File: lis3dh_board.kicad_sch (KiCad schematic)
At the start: 19 parts, among them J1 T4_IF, J2 BQ25798_BOARD, J3 WL-125, Q1 BSS138, U1 TLV75530PDBV, U2 LIS3DH

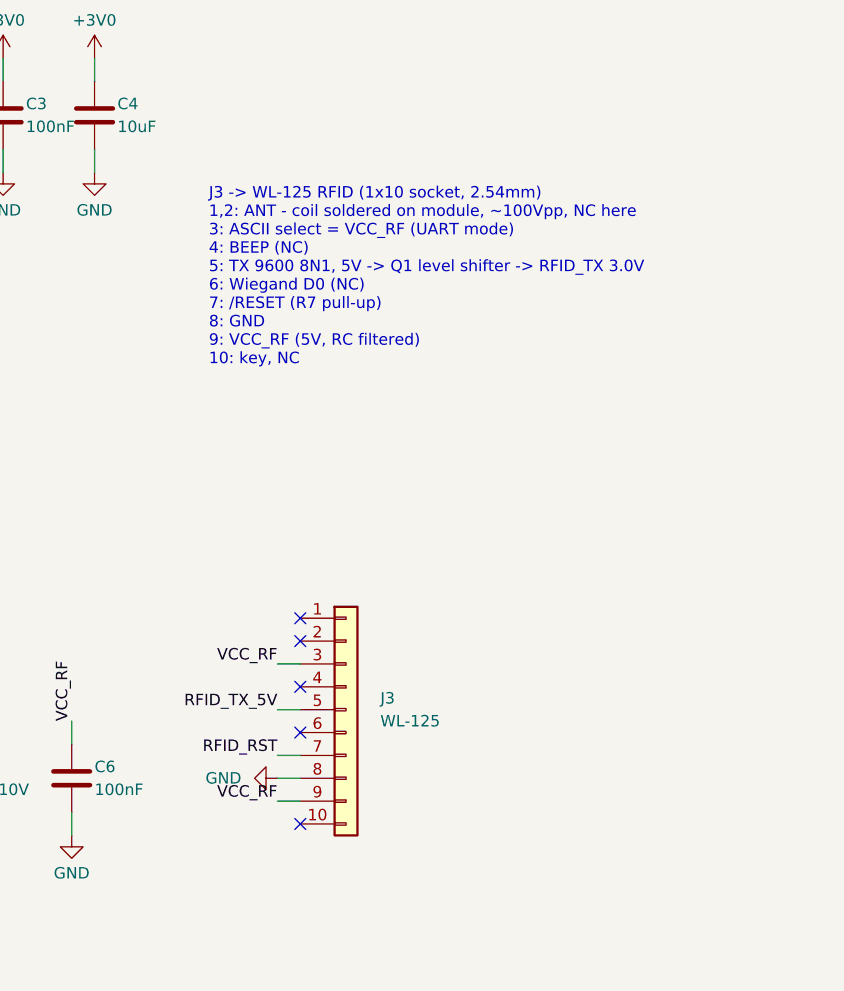
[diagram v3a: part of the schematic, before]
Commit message: Put the WL-125 polarization key next to module pin 1
J3 pin 1 is now the key position and module pins 1-9 map to J3 pins
2-10, matching how the module's 10-pin header is fitted.

Co-Authored-By: Claude Opus 5.5 <noreply@anthropic.com>
Claude-Session: https://claude.ai/code/session_012K15v8QNdkAoa4NiCNiWuG
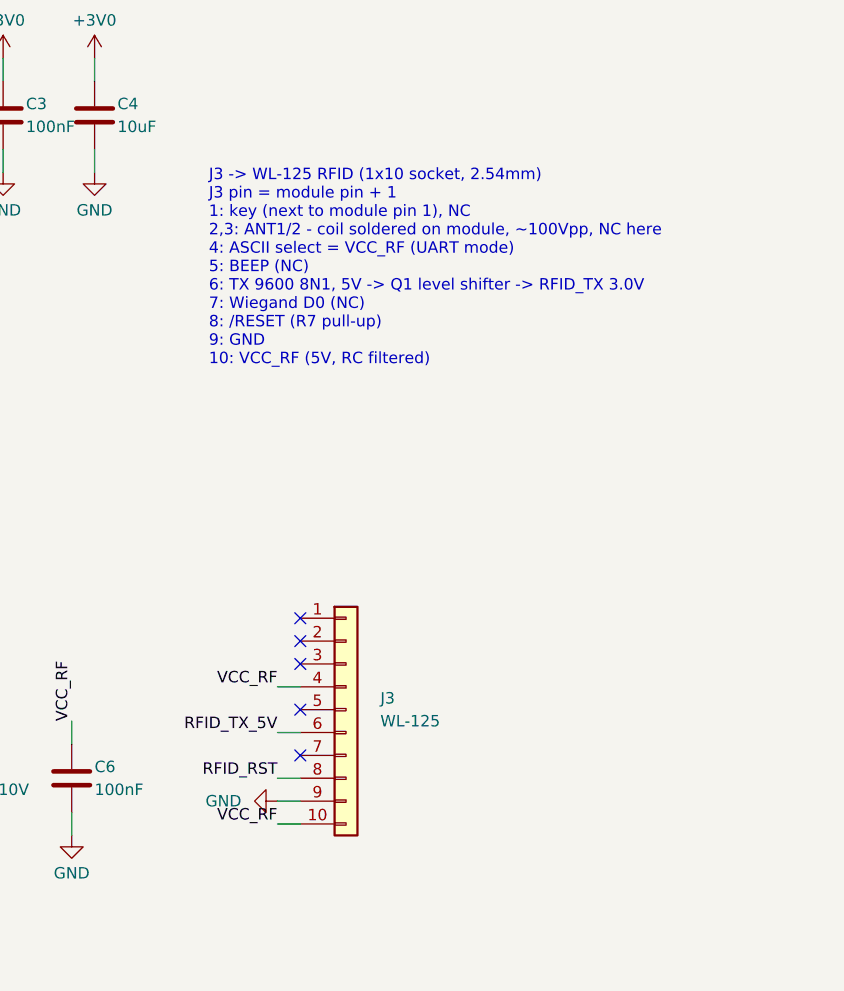
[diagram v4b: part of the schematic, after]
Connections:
- net GND: now also J3.9 (Pin_9); no longer J3.8 (Pin_8)
- net RFID_RST: now also J3.8 (Pin_8); no longer J3.7 (Pin_7)
- net RFID_TX_5V: now also J3.6 (Pin_6); no longer J3.5 (Pin_5)
- net VCC_RF: now also J3.10 (Pin_10), J3.4 (Pin_4); no longer J3.3 (Pin_3), J3.9 (Pin_9)
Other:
- note added: "J3 -> WL-125 RFID (1x10 socket, 2.54mm) J3 pin = module pin + 1 1: key (next to module pin 1), NC 2,3: ANT1/2 - coil soldered on module, ~100Vpp, NC here 4: ASCII select = VCC_RF (UART mode) 5: BEEP (NC) 6: TX 9600 8N1, 5V -> Q1 level shifter -> RFID_TX 3.0V 7: Wiegand D0 (NC) 8: /RESET (R7 pull-up) 9: GND 10: VCC_RF (5V, RC filtered)"
- note removed: "J3 -> WL-125 RFID (1x10 socket, 2.54mm) 1,2: ANT - coil soldered on module, ~100Vpp, NC here 3: ASCII select = VCC_RF (UART mode) 4: BEEP (NC) 5: TX 9600 8N1, 5V -> Q1 level shifter -> RFID_TX 3.0V 6: Wiegand D0 (NC) 7: /RESET (R7 pull-up) 8: GND 9: VCC_RF (5V, RC filtered) 10: key, NC"
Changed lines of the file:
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@@
   (no_connect (at 223.52 134.62))
   (no_connect (at 223.52 137.16))
-  (wire (pts (xy 223.52 139.7) (xy 220.98 139.7))
+  (no_connect (at 223.52 139.7))
+  (wire (pts (xy 223.52 142.24) (xy 220.98 142.24))
     (stroke (width 0) (type default))
   )
-  (label "VCC_RF" (at 220.98 139.7 180) (fields_autoplaced)
+  (label "VCC_RF" (at 220.98 142.24 180) (fields_autoplaced)
     (effects (font (size 1.27 1.27)) (justify right bottom))
   )
-  (no_connect (at 223.52 142.24))
-  (wire (pts (xy 223.52 144.78) (xy 220.98 144.78))
+  (no_connect (at 223.52 144.78))
+  (wire (pts (xy 223.52 147.32) (xy 220.98 147.32))
     (stroke (width 0) (type default))
   )
-  (label "RFID_TX_5V" (at 220.98 144.78 180) (fields_autoplaced)
+  (label "RFID_TX_5V" (at 220.98 147.32 180) (fields_autoplaced)
     (effects (font (size 1.27 1.27)) (justify right bottom))
   )
-  (no_connect (at 223.52 147.32))
-  (wire (pts (xy 223.52 149.86) (xy 220.98 149.86))
-    (stroke (width 0) (type default))
-  )
-  (label "RFID_RST" (at 220.98 149.86 180) (fields_autoplaced)
-    (effects (font (size 1.27 1.27)) (justify right bottom))
-  )
+  (no_connect (at 223.52 149.86))
   (wire (pts (xy 223.52 152.4) (xy 220.98 152.4))
     (stroke (width 0) (type default))
   )
-  (symbol (lib_id "power:GND") (at 220.98 152.4 270) (unit 1)
+  (label "RFID_RST" (at 220.98 152.4 180) (fields_autoplaced)
+    (effects (font (size 1.27 1.27)) (justify right bottom))
+  )
+  (wire (pts (xy 223.52 154.94) (xy 220.98 154.94))
+    (stroke (width 0) (type default))
+  )
+  (symbol (lib_id "power:GND") (at 220.98 154.94 270) (unit 1)
     (in_bom no) (on_board no) (dnp no)
-    (property "Reference" "#PWR019" (at 220.98 158.4 0)
+    (property "Reference" "#PWR019" (at 220.98 160.94 0)
       (effects (font (size 1.27 1.27)) hide)
     )
-    (property "Value" "GND" (at 216.98 152.4 270)
+    (property "Value" "GND" (at 216.98 154.94 270)
       (effects (font (size 1.27 1.27)) (justify left))
     )
-    (property "Footprint" "" (at 220.98 152.4 0)
+    (property "Footprint" "" (at 220.98 154.94 0)
       (effects (font (size 1.27 1.27)) hide)
     )
-    (property "Datasheet" "~" (at 220.98 152.4 0)
+    (property "Datasheet" "~" (at 220.98 154.94 0)
       (effects (font (size 1.27 1.27)) hide)
     )
@@
     )
   )
-  (wire (pts (xy 223.52 154.94) (xy 220.98 154.94))
+  (wire (pts (xy 223.52 157.48) (xy 220.98 157.48))
     (stroke (width 0) (type default))
   )
-  (label "VCC_RF" (at 220.98 154.94 180) (fields_autoplaced)
+  (label "VCC_RF" (at 220.98 157.48 180) (fields_autoplaced)
     (effects (font (size 1.27 1.27)) (justify right bottom))
   )
-  (no_connect (at 223.52 157.48))
-  (text "J3 -> WL-125 RFID (1x10 socket, 2.54mm)\n1,2: ANT - coil soldered on module, ~100Vpp, NC here\n3: ASCII select = VCC_RF (UART mode)\n4: BEEP (NC)\n5: TX 9600 8N1, 5V -> Q1 level shifter -> RFID_TX 3.0V\n6: Wiegand D0 (NC)\n7: /RESET (R7 pull-up)\n8: GND\n9: VCC_RF (5V, RC filtered)\n10: key, NC" (at 213.36 106.68 0)
+  (text "J3 -> WL-125 RFID (1x10 socket, 2.54mm)\nJ3 pin = module pin + 1\n1: key (next to module pin 1), NC\n2,3: ANT1/2 - coil soldered on module, ~100Vpp, NC here\n4: ASCII select = VCC_RF (UART mode)\n5: BEEP (NC)\n6: TX 9600 8N1, 5V -> Q1 level shifter -> RFID_TX 3.0V\n7: Wiegand D0 (NC)\n8: /RESET (R7 pull-up)\n9: GND\n10: VCC_RF (5V, RC filtered)" (at 213.36 106.68 0)
     (effects (font (size 1.27 1.27)) (justify left bottom))
   )

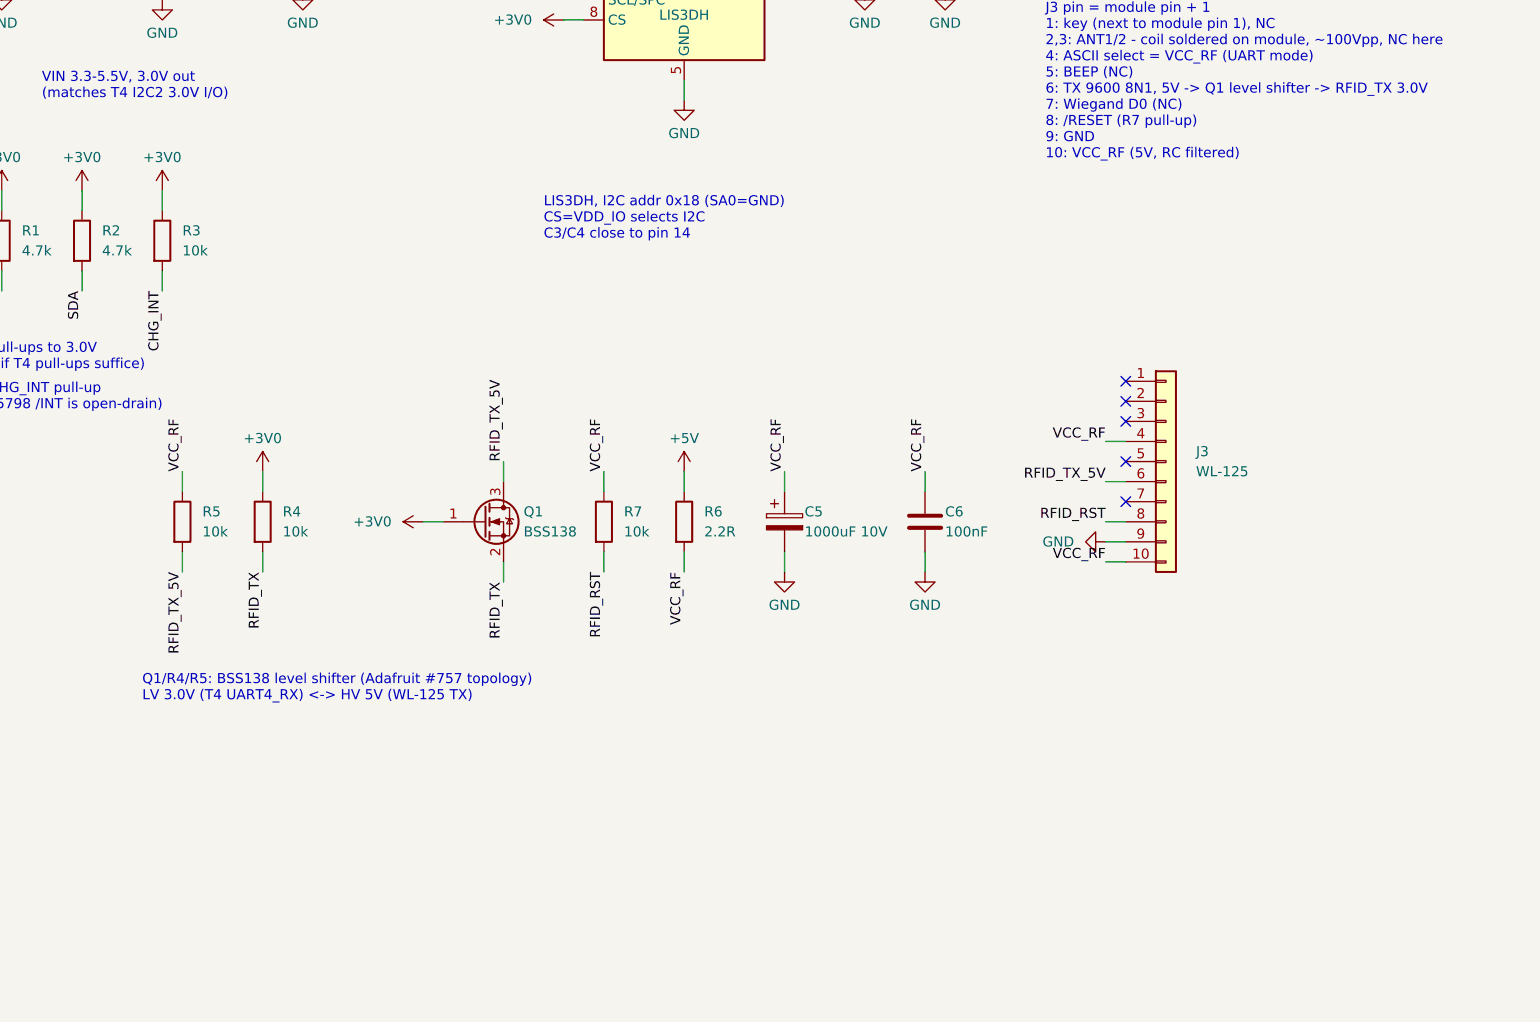
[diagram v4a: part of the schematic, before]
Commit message: Use a 3-stage RC filter for the WL-125 supply
+5V -> 4.7R -> 1000uF -> 1R -> 1000uF -> 1R -> 1000uF + 100nF ->
VCC_RF, following the WL-125 datasheet appendix. The first resistor is
4.7R to keep the inrush into 3 x 1000uF around 1A, and the 100nF covers
frequencies where the electrolytics stop working. Sheet moved to A3 to
fit the filter.

Co-Authored-By: Claude Opus 5.5 <noreply@anthropic.com>
Claude-Session: https://claude.ai/code/session_012K15v8QNdkAoa4NiCNiWuG
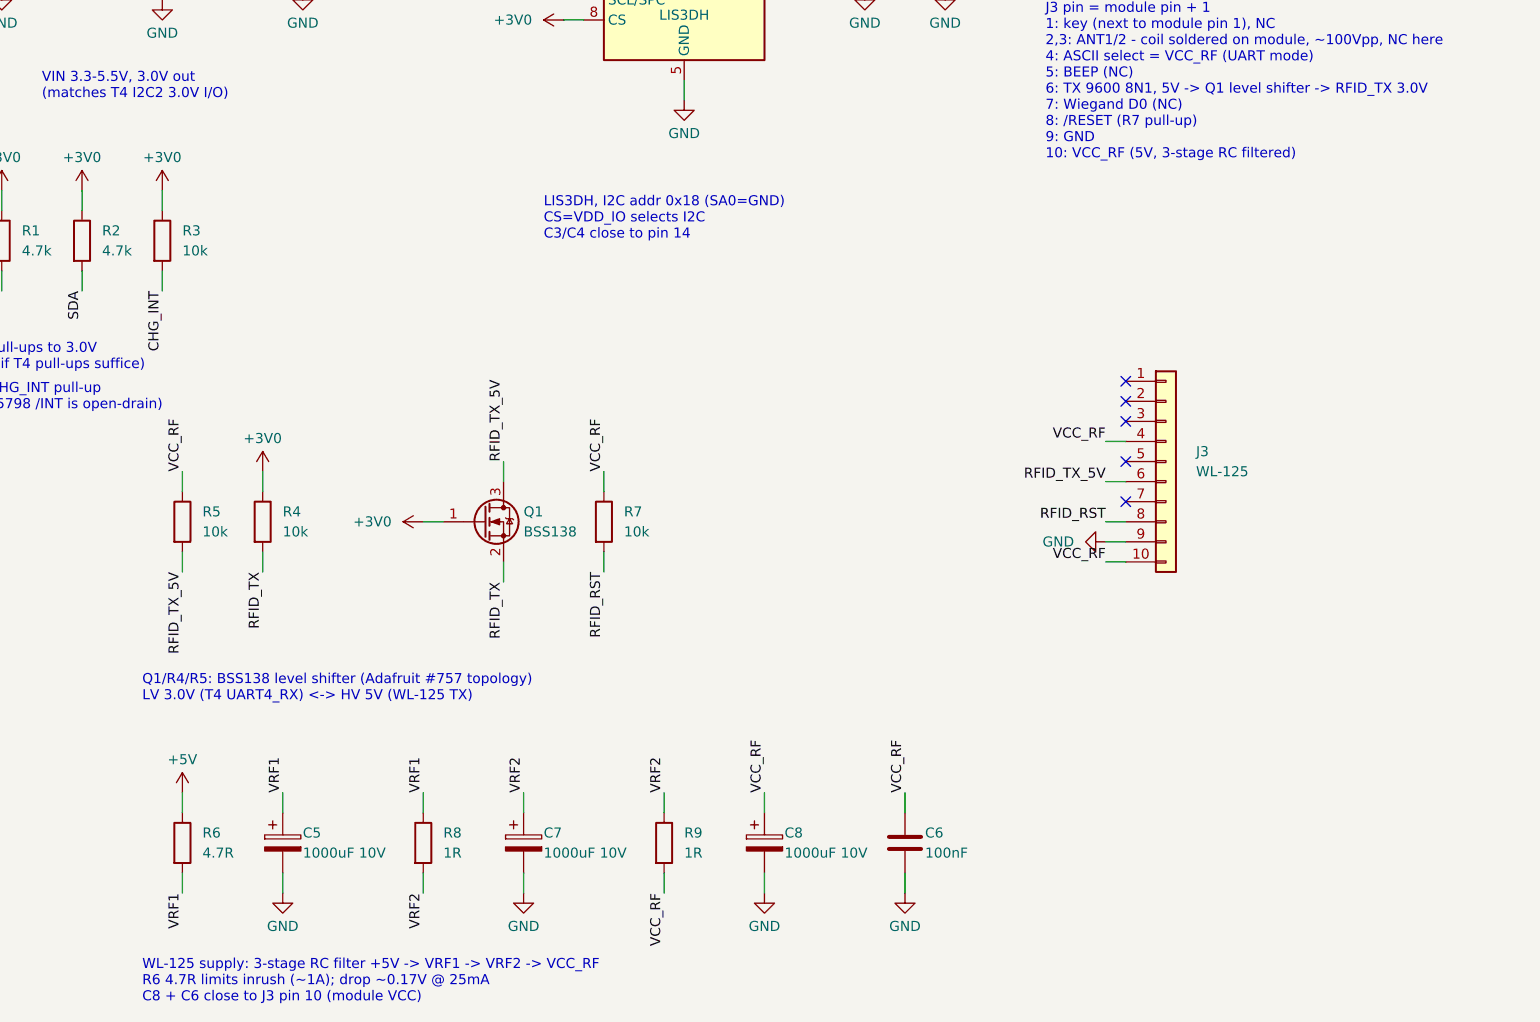
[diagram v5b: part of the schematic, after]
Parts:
- added C6: 100nF, Capacitor_SMD:C_0603_1608Metric, symbol Device:C
- added C7: 1000uF 10V, Capacitor_THT:CP_Radial_D10.0mm_P5.00mm, symbol Device:C_Polarized
- added R9: 1R, Resistor_SMD:R_0805_2012Metric, symbol Device:R
- added U2: LIS3DH, Package_LGA:LGA-16_3x3mm_P0.5mm_LayoutBorder3x5y, symbol Sensor_Motion:LIS3DH
- C8: renamed from U2; value LIS3DH -> 1000uF 10V; footprint Package_LGA:LGA-16_3x3mm_P0.5mm_LayoutBorder3x5y -> Capacitor_THT:CP_Radial_D10.0mm_P5.00mm; symbol Sensor_Motion:LIS3DH -> Device:C_Polarized
- R6: value 2.2R -> 4.7R
- R8: renamed from C6; value 100nF -> 1R; footprint Capacitor_SMD:C_0603_1608Metric -> Resistor_SMD:R_0805_2012Metric; symbol Device:C -> Device:R
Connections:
- net +3V0: now also U2.1 (VDD_IO), U2.14 (VDD), U2.8 (CS); no longer C8.1 (VDD_IO), C8.14 (VDD), C8.8 (CS)
- net GND: now also C8.2, C6.2, C7.2, U2.10 (GND), U2.12 (GND), U2.5 (GND), U2.7 (SDO/SA0); no longer C8.10 (GND), C8.12 (GND), C8.5 (GND), C8.7 (SDO/SA0), R8.2
- net INT1: now also U2.11 (INT1); no longer C8.11 (INT1)
- net SCL: now also U2.4 (SCL/SPC); no longer C8.4 (SCL/SPC)
- net SDA: now also U2.6 (SDA/SDI/SDO); no longer C8.6 (SDA/SDI/SDO)
- net VCC_RF: now also C8.1, C6.1, R9.2; no longer C5.1, R6.2, R8.1
- new net VRF1: C5.1, R6.2, R8.1
- new net VRF2: C7.1, R8.2, R9.1
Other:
- note added: "J3 -> WL-125 RFID (1x10 socket, 2.54mm) J3 pin = module pin + 1 1: key (next to module pin 1), NC 2,3: ANT1/2 - coil soldered on module, ~100Vpp, NC here 4: ASCII select = VCC_RF (UART mode) 5: BEEP (NC) 6: TX 9600 8N1, 5V -> Q1 level shifter -> RFID_TX 3.0V 7: Wiegand D0 (NC) 8: /RESET (R7 pull-up) 9: GND 10: VCC_RF (5V, 3-stage RC filtered)"
- note added: "WL-125 supply: 3-stage RC filter +5V -> VRF1 -> VRF2 -> VCC_RF R6 4.7R limits inrush (~1A); drop ~0.17V @ 25mA C8 + C6 close to J3 pin 10 (module VCC)"
- note removed: "J3 -> WL-125 RFID (1x10 socket, 2.54mm) J3 pin = module pin + 1 1: key (next to module pin 1), NC 2,3: ANT1/2 - coil soldered on module, ~100Vpp, NC here 4: ASCII select = VCC_RF (UART mode) 5: BEEP (NC) 6: TX 9600 8N1, 5V -> Q1 level shifter -> RFID_TX 3.0V 7: Wiegand D0 (NC) 8: /RESET (R7 pull-up) 9: GND 10: VCC_RF (5V, RC filtered)"
- moved on the sheet: C5, R6

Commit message: Use Panasonic EEE-FT1A102AP for the RFID filter capacitors
C5/C7/C8 move from 10mm radial THT to SMD 8x10.2mm (CP_Elec_8x10.5),
with MPN and LCSC part number (C278408) set on the symbols and in the
BOM. EEE-FK1A102P is noted as a fallback; it needs the 10x10.5 footprint.

Co-Authored-By: Claude Opus 5.5 <noreply@anthropic.com>
Claude-Session: https://claude.ai/code/session_012K15v8QNdkAoa4NiCNiWuG
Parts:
- C5, C7, C8: footprint Capacitor_THT:CP_Radial_D10.0mm_P5.00mm -> Capacitor_SMD:CP_Elec_8x10.5; LCSC (none) -> C278408; MPN (none) -> Panasonic EEE-FT1A102AP
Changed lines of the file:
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@@
       (effects (font (size 1.27 1.27)) (justify left))
     )
-    (property "Footprint" "Capacitor_THT:CP_Radial_D10.0mm_P5.00mm" (at 116.84 193.04 0)
+    (property "Footprint" "Capacitor_SMD:CP_Elec_8x10.5" (at 116.84 193.04 0)
       (effects (font (size 1.27 1.27)) hide)
     )
     (property "Datasheet" "~" (at 116.84 193.04 0)
+      (effects (font (size 1.27 1.27)) hide)
+    )
+    (property "MPN" "Panasonic EEE-FT1A102AP" (at 116.84 193.04 0)
+      (effects (font (size 1.27 1.27)) hide)
+    )
+    (property "LCSC" "C278408" (at 116.84 193.04 0)
       (effects (font (size 1.27 1.27)) hide)
     )
@@
       (effects (font (size 1.27 1.27)) (justify left))
     )
-    (property "Footprint" "Capacitor_THT:CP_Radial_D10.0mm_P5.00mm" (at 147.32 193.04 0)
+    (property "Footprint" "Capacitor_SMD:CP_Elec_8x10.5" (at 147.32 193.04 0)
       (effects (font (size 1.27 1.27)) hide)
     )
     (property "Datasheet" "~" (at 147.32 193.04 0)
+      (effects (font (size 1.27 1.27)) hide)
+    )
+    (property "MPN" "Panasonic EEE-FT1A102AP" (at 147.32 193.04 0)
+      (effects (font (size 1.27 1.27)) hide)
+    )
+    (property "LCSC" "C278408" (at 147.32 193.04 0)
       (effects (font (size 1.27 1.27)) hide)
     )
@@
       (effects (font (size 1.27 1.27)) (justify left))
     )
-    (property "Footprint" "Capacitor_THT:CP_Radial_D10.0mm_P5.00mm" (at 177.8 193.04 0)
+    (property "Footprint" "Capacitor_SMD:CP_Elec_8x10.5" (at 177.8 193.04 0)
       (effects (font (size 1.27 1.27)) hide)
     )
@@
       (effects (font (size 1.27 1.27)) hide)
     )
+    (property "MPN" "Panasonic EEE-FT1A102AP" (at 177.8 193.04 0)
+      (effects (font (size 1.27 1.27)) hide)
+    )
+    (property "LCSC" "C278408" (at 177.8 193.04 0)
+      (effects (font (size 1.27 1.27)) hide)
+    )
